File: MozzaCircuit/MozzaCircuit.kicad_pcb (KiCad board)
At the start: 2 copper layers, 183 x 128.1 mm, 174 parts, among them J1 8P8C_both_sides, SW13 SW_ChocV2_rev, SW14 SW_ChocV2_rev, SW15 SW_ChocV2_rev, SW21 SW_ChocV2_rev, SW22 SW_ChocV2_rev, SW23 SW_ChocV2_rev, SW24 SW_ChocV2_rev, SW25 SW_ChocV2_rev, SW31 SW_ChocV2_rev, SW32 SW_ChocV2_rev, SW33 SW_ChocV2_rev, SW34 SW_ChocV2_rev, SW35 SW_ChocV2_rev, SW41 SW_ChocV2_rev, SW42 SW_ChocV2_rev, SW43 SW_ChocV2_rev, SW44 SW_ChocV2_rev, SW51 SW_ChocV2_rev, SW52 SW_ChocV2_rev, SW53 SW_ChocV2_rev, SW54 SW_ChocV2_rev, SW61 SW_ChocV2_rev, SW62 SW_ChocV2_rev, SW63 SW_ChocV2_rev, SW64 SW_ChocV2_rev, SW71 SW_ChocV2_rev, SW72 SW_ChocV2_rev, SW73 SW_ChocV2_rev, SW82 SW_ChocV2_rev, SW83 SW_ChocV2_rev, SW84 SW_ChocV2_rev, U1 MCP23017_ML, U2 MCP23017_ML_NoTP

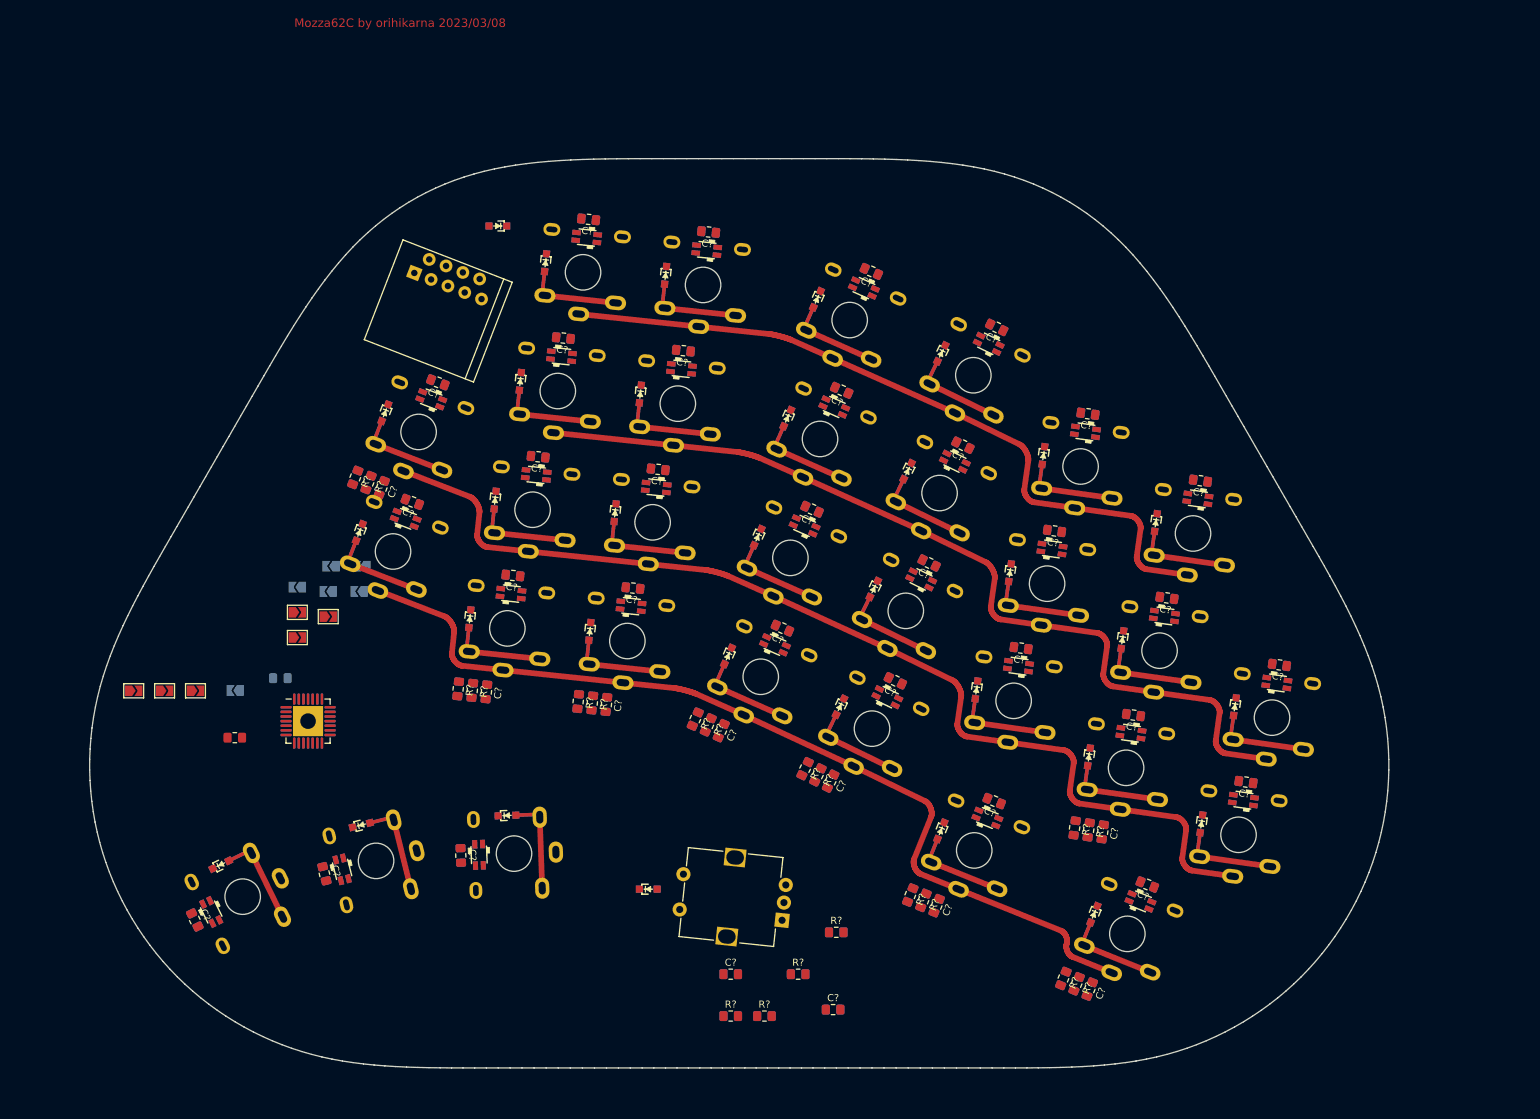
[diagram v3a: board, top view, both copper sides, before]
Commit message: led wiring
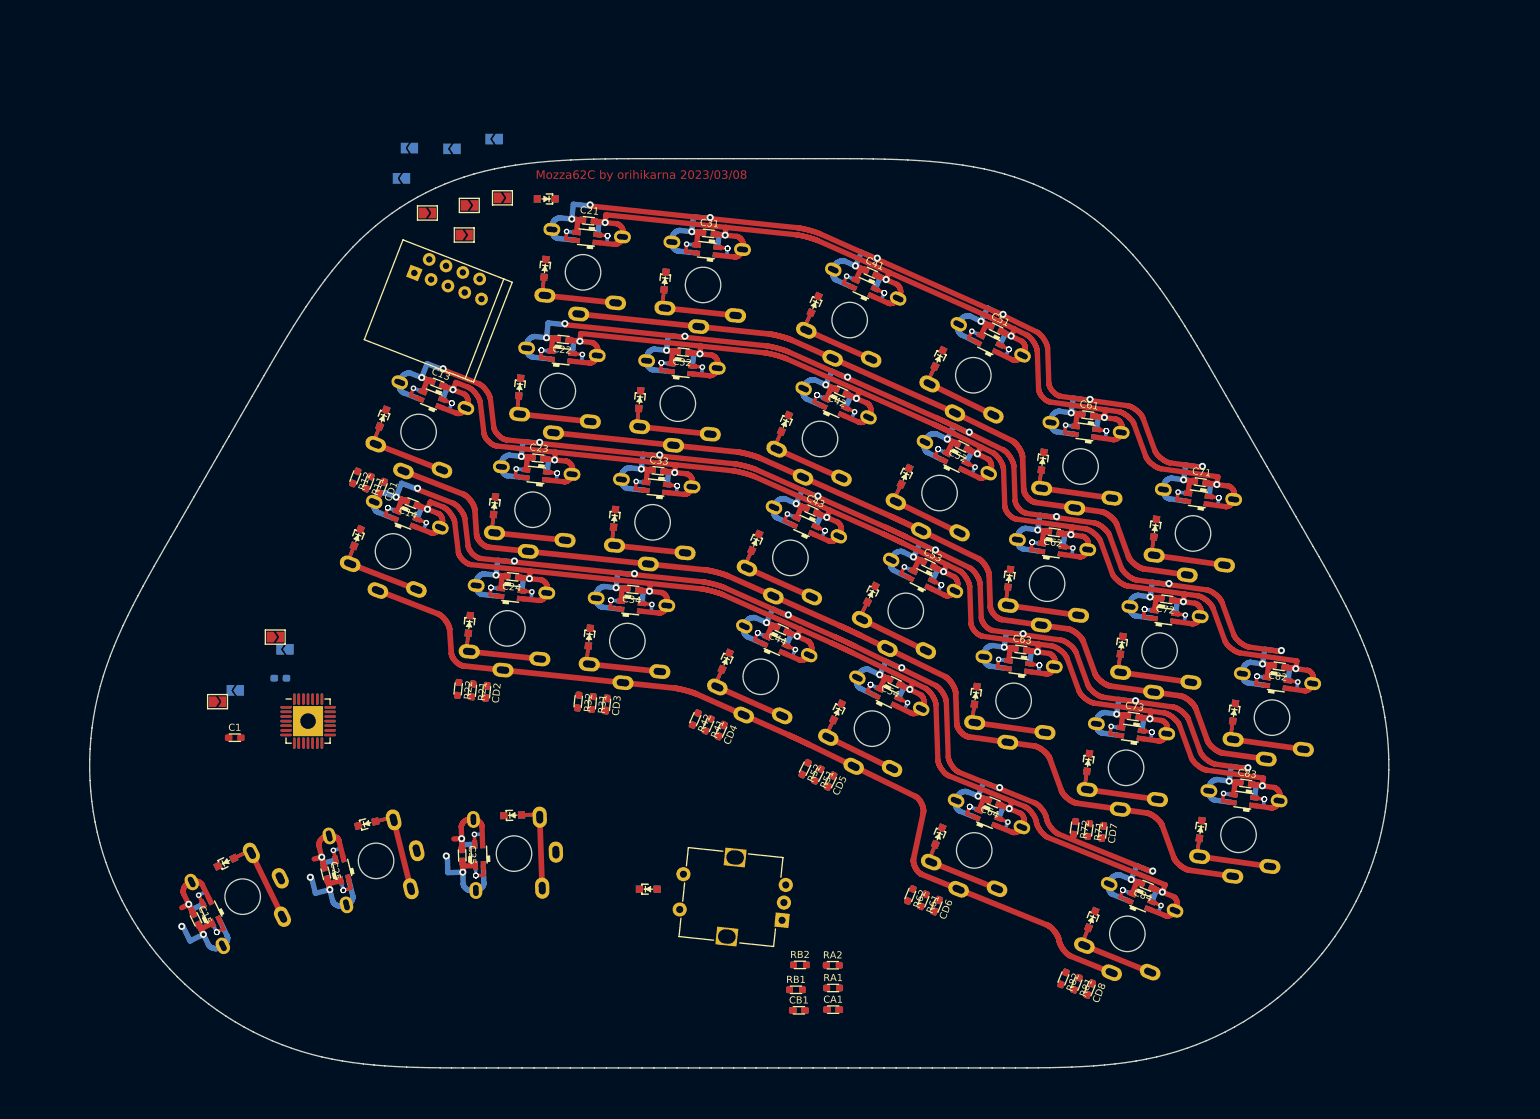
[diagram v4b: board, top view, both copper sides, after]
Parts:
- C1, C2: footprint 00_KeyParts:C_2012 -> 00_KeyParts:C_1608_HandSolder
- C13, C14, C15, C21, C22, C23, C24, C25, C31, C32, C33, C34, C35, C41, C42, C43, C44, C51, C52, C53, C54, C61, C62, C63, C64, C71, C72, C73, C82, C83, C84, CA1, CB1, CD1, CD2, CD3, CD4, CD5, CD6, CD7, CD8: footprint 00_KeyParts:C_2012_rev -> 00_KeyParts:C_1608_HandSolder_both_sides
- R11, R12, R21, R22, R31, R32, R41, R42, R51, R52, R61, R62, R71, R72, R81, R82, RA1, RA2, RB1, RB2: footprint 00_KeyParts:R_2012_rev -> 00_KeyParts:R_1608_HandSolder_both_sides
- moved JPF8 74.8 mm to (90.4, 29.4)
- moved JPB4 68.9 mm to (99.8, 18.9)
- moved JPB2 64.7 mm to (93.8, 20.3)
- moved JPF4 63.9 mm to (100.9, 27.2)
- moved JPF6 62.2 mm to (96.3, 28.3)
- moved JPF2 61.4 mm to (95.6, 32.5)
- moved JPB6 59.3 mm to (87.8, 20.2)
- moved JPB8 55.5 mm to (86.7, 24.5)
- moved JPF3 17.3 mm to (68.9, 89.1)
- moved RA2 16.1 mm to (147.5, 135.3)
- moved JPB3 13.3 mm to (70.3, 90.8)
- moved JPF7 11.9 mm to (60.8, 98.2)
- moved CB1 10.9 mm to (142.7, 141.7)
- moved RB1 9.89 mm to (142.3, 138.8)
- moved RB2 8.78 mm to (142.8, 135.3)
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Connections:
- C21 pad 1: 5VD -> 4V3D
- SW13 pad 4: 5VD -> GNDD
- SW13 pad 5: GNDD -> 5VD
- SW21 pad 4: 5VD -> GNDD
- SW21 pad 5: GNDD -> 4V3D
- SW23 pad 4: 5VD -> GNDD
- SW23 pad 5: GNDD -> 5VD
- SW31 pad 4: 5VD -> GNDD
- SW31 pad 5: GNDD -> 5VD
- SW33 pad 4: 5VD -> GNDD
- SW33 pad 5: GNDD -> 5VD
- SW41 pad 4: 5VD -> GNDD
- SW41 pad 5: GNDD -> 5VD
- SW43 pad 4: 5VD -> GNDD
- SW43 pad 5: GNDD -> 5VD
- SW51 pad 4: 5VD -> GNDD
- SW51 pad 5: GNDD -> 5VD
- SW53 pad 4: 5VD -> GNDD
- SW53 pad 5: GNDD -> 5VD
- SW61 pad 4: 5VD -> GNDD
- SW61 pad 5: GNDD -> 5VD
- SW63 pad 4: 5VD -> GNDD
- SW63 pad 5: GNDD -> 5VD
- SW71 pad 4: 5VD -> GNDD
- SW71 pad 5: GNDD -> 5VD
- SW73 pad 4: 5VD -> GNDD
- SW73 pad 5: GNDD -> 5VD
- SW83 pad 4: 5VD -> GNDD
- SW83 pad 5: GNDD -> 5VD
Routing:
- net GNDD: track 0.00 -> 1051.7 mm, vias 0 -> 48
- net 5VD: track 0.00 -> 1003.8 mm, vias 0 -> 43
- net 4V3D: track 0.00 -> 36.8 mm, vias 0 -> 2
- net Net-(L21-Pad1): track 0.00 -> 7.80 mm, vias 0 -> 4
- net Net-(L23-Pad1): track 0.00 -> 7.80 mm, vias 0 -> 4
- net Net-(L24-Pad3): track 0.00 -> 7.80 mm, vias 0 -> 4
- net Net-(L22-Pad3): track 0.00 -> 7.80 mm, vias 0 -> 4
- net Net-(L14-Pad3): track 0.00 -> 7.80 mm, vias 0 -> 4
- net Net-(L13-Pad1): track 0.00 -> 7.80 mm, vias 0 -> 4
- net Net-(L15-Pad1): track 0.00 -> 7.80 mm, vias 0 -> 4
- net Net-(L54-Pad3): track 0.00 -> 7.80 mm, vias 0 -> 4
- net Net-(L13-Pad3): track 0.00 -> 7.80 mm, vias 0 -> 4
- net Net-(L33-Pad1): track 0.00 -> 7.80 mm, vias 0 -> 4
- net Net-(L32-Pad3): track 0.00 -> 7.80 mm, vias 0 -> 4
- net Net-(L34-Pad3): track 0.00 -> 7.80 mm, vias 0 -> 4
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
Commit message: added power cap
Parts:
- removed CA1: 33n, 00_KeyParts:C_1608_HandSolder_both_sides
- removed CB1: C_Small, 00_KeyParts:C_1608_HandSolder_both_sides
- removed D45: D_Small, 00_KeyParts:D_SOD-323_both_sides
- removed JPB3, JPB7, JPF3, JPF7: SolderJumper_2_Open, Jumper:SolderJumper-2_P1.3mm_Open_TrianglePad1.0x1.5mm
- removed RA1: 10k, 00_KeyParts:R_1608_HandSolder_both_sides
- removed RA2: 4k7, 00_KeyParts:R_1608_HandSolder_both_sides
- removed RB1, RB2: R_Small_US, 00_KeyParts:R_1608_HandSolder_both_sides
- added C3: C_Small, 00_KeyParts:C_1608_HandSolder_both_sides, F.Cu at (80.3, 40.1)
- added C4: C_Small, 00_KeyParts:C_1608_HandSolder_both_sides, F.Cu at (67.4, 88.7)
- added CD11: 33n, 00_KeyParts:C_1608_HandSolder_both_sides, F.Cu at (119.5, 120.8)
- added CD12: C_Small, 00_KeyParts:C_1608_HandSolder_both_sides, F.Cu at (118.7, 127.7)
- added D65: D_Small, 00_KeyParts:D_SOD-323_both_sides, F.Cu at (143.6, 126.8)
- added R1: 100, 00_KeyParts:R_1608_HandSolder_both_sides, F.Cu at (65.0, 87.8)
- added R111: 10k, 00_KeyParts:R_1608_HandSolder_both_sides, F.Cu at (121.1, 120.9)
- added R112: 4k7, 00_KeyParts:R_1608_HandSolder_both_sides, F.Cu at (122.7, 121.1)
- added R121: R_Small_US, 00_KeyParts:R_1608_HandSolder_both_sides, F.Cu at (120.3, 127.9)
- added R122: R_Small_US, 00_KeyParts:R_1608_HandSolder_both_sides, F.Cu at (121.9, 128.1)
- J1: moved to B.Cu
- JPB2, JPB4, JPB6, JPB8, JPF2, JPF4, JPF6, JPF8: footprint Jumper:SolderJumper-2_P1.3mm_Open_TrianglePad1.0x1.5mm -> 00_KeyParts:SolderJumper-2_P1.3mm_Open_TrianglePad1.0x1.5mm
- moved R12 22.8 mm to (85.5, 88.8), turned to 68.8 degrees
- moved R11 20.7 mm to (83.4, 88.0)
- moved CD7 20.7 mm to (173.7, 133.6), turned to -112 degrees
- moved R71 20.3 mm to (171.6, 132.7), turned to -112 degrees
- moved R72 19.9 mm to (169.6, 131.9), turned to 68 degrees
- moved CD1 19.3 mm to (81.4, 87.2)
- moved JPB6 15.4 mm to (96.3, 33.1), turned to 68.8 degrees
- moved JPB8 15.2 mm to (98.6, 34.0), turned to 68.8 degrees
- moved C1 14.5 mm to (69.5, 90.2), turned to 158.8 degrees
- moved JPB4 14.5 mm to (93.9, 32.2), turned to 68.8 degrees
- moved JPB2 11.2 mm to (91.5, 31.3), turned to 68.8 degrees
- moved D14 10.8 mm to (90.6, 79.0)
- moved D13 10.8 mm to (94.2, 62.2)
- moved D34 10.8 mm to (123.9, 90.2)
- moved D21 10.8 mm to (117.7, 38.3)
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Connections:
- J1 pad 3: Net-(J1-Pad3) -> SCK_SDA
- J1 pad 5: 5VD -> NRST_in
- J1 pad 7: Net-(J1-Pad7) -> SDA_SCK
- JPB2 pad 2: GND -> GNDD
- JPB4 pad 2: GNDD -> 5VD
- JPB6 pad 2: NRST -> GND
- JPB8 pad 2: SDA -> 3V3
- JPF2 pad 2: GND -> GNDD
- JPF4 pad 2: GNDD -> 5VD
- JPF6 pad 2: NRST -> GND
- JPF8 pad 2: SDA -> 3V3
- SW14 pad 4: unconnected-(SW14-Pad4) -> 5VD
- SW14 pad 5: unconnected-(SW14-Pad5) -> GNDD
- SW15 pad 1: Net-(D15-Pad2) -> ROW5
- SW15 pad 2: ROW5 -> Net-(D15-Pad2)
- SW15 pad 3: ROW5 -> Net-(D15-Pad2)
- SW15 pad 4: GNDD -> 5VD
- SW15 pad 5: 5VD -> GNDD
- SW25 pad 4: 5VD -> GNDD
- SW25 pad 5: GNDD -> 5VD
- U1 pad 1: ROW5 -> ROW1
- U1 pad 11: GND -> 3V3
- U1 pad 17: COL1 -> unconnected-(U1-Pad17)
- U1 pad 18: COL2 -> ROW5
- U1 pad 19: COL3 -> COLB
- U1 pad 2: REA -> COL1
- U1 pad 20: COL4 -> COLA
- U1 pad 21: COL5 -> COL8
- U1 pad 22: COL6 -> COL7
- U1 pad 23: COL7 -> COL6
- U1 pad 24: COL8 -> COL5
- U1 pad 25: ROW1 -> COL4
- U1 pad 26: ROW2 -> COL3
- U1 pad 27: ROW3 -> COL2
- U1 pad 28: ROW4 -> ROW2
- U1 pad 3: REB -> ROW4
- U1 pad 4: unconnected-(U1-Pad4) -> ROW3
- U1 pad 8: SCK -> SCK_SDA
- U1 pad 9: SDA -> SDA_SCK
- U2 pad 1: ROW5 -> COL8
- U2 pad 11: 3V3 -> GND
- U2 pad 17: COL1 -> unconnected-(U2-Pad17)
- U2 pad 18: COL2 -> ROW3
- U2 pad 19: COL3 -> ROW4
- U2 pad 2: REA -> COLA
- U2 pad 20: COL4 -> COL1
- U2 pad 21: COL5 -> ROW1
- U2 pad 22: COL6 -> ROW2
- U2 pad 23: COL7 -> COL2
- U2 pad 24: COL8 -> COL3
- U2 pad 25: ROW1 -> COL4
- U2 pad 26: ROW2 -> COL5
- U2 pad 27: ROW3 -> COL6
- U2 pad 28: ROW4 -> COL7
- U2 pad 3: REB -> COLB
- U2 pad 4: unconnected-(U2-Pad4) -> ROW5
- U2 pad 8: SCK -> SDA_SCK
- U2 pad 9: SDA -> SCK_SDA
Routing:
- net GND: track 0.00 -> 1442.4 mm, vias 0 -> 52
- net 3V3: track 0.00 -> 397.3 mm, vias 0 -> 26
- net 5VD: track 1003.8 -> 1331.6 mm, vias 43 -> 62
- net GNDD: track 1051.7 -> 1358.4 mm, vias 48 -> 63
- net Net-(D21-Pad1): track 0.00 -> 161.2 mm, vias 0 -> 6
- net Net-(D31-Pad1): track 0.00 -> 157.7 mm, vias 0 -> 6
- net COL8: track 0.00 -> 145.5 mm, vias 0 -> 2
- net ROW5: track 10.00 -> 153.5 mm, vias 0 -> 1
- net Net-(D61-Pad1): track 0.00 -> 143.2 mm, vias 0 -> 6
- net COL7: track 0.00 -> 130.2 mm, vias 0 -> 2
- net Net-(D51-Pad1): track 0.00 -> 120.3 mm, vias 0 -> 5
- net Net-(D41-Pad1): track 0.00 -> 120.3 mm, vias 0 -> 5
- net COL6: track 0.00 -> 119.4 mm, vias 0 -> 2
- net Net-(D71-Pad1): track 0.00 -> 110.6 mm, vias 0 -> 4
- net Net-(D13-Pad1): track 0.00 -> 110.3 mm, vias 0 -> 4
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- added copper zone on B.Cu, net GND
- added copper zone on F.Cu, net GND
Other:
- board size 183 x 128.1 mm -> 187.1 x 130.3 mm
- board text removed: "Mozza62C by orihikarna 2023/03/08"
